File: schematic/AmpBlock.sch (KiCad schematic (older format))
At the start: 9 parts, among them U1 OPA454AIDDAR

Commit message: Added connectors to the library and made an array of lots of amps
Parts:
- renumbered C1 to C29, C3 to C30, C2 to C31, C4 to C32, R4 to R29, R5 to R30, R6 to R31, R7 to R32, U1 to U8
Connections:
- net labels added: INPUT_COM, OUTPUT_COM
- wire segments 32 -> 38
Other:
- note added: "In the LL schematic, the ground reference of the supply bypass capacitors are both what I call input_com\n"
- note added: "Should the E/D com also go to the local ground?"
- moved on the sheet: C3, R2

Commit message: Started adding footprints to library and started working on the layout of the amplifier block
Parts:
- C29, C30, C31, C32: footprint (none) -> Capacitor_SMD:C_0603_1608Metric
- R29, R30, R31, R32: footprint (none) -> Resistor_SMD:R_0603_1608Metric
- U8: footprint (none) -> ARTIQAmp:TI_SO-PowerPAD-8_ThermalVias
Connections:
- wire segments 38 -> 42
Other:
- moved on the sheet: C1, R1, R2
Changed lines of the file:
@@
 EESchema Schematic File Version 4
-LIBS:ARTIQAmp-cache
 EELAYER 29 0
 EELAYER END
 $Descr A4 11693 8268
 encoding utf-8
-Sheet 2 33
+Sheet 1 1
 Title "Amplifier block"
 Date ""
@@
 L Device:R R29
 U 1 1 5C968DBB
-P 4350 3350
+P 4300 3350
 AR Path="/5C968447/5C968DBB" Ref="R29"  Part="1"
 AR Path="/5C98A5A9/5C968DBB" Ref="R?"  Part="1"
@@
 AR Path="/5CAE2E6A/5C968DBB" Ref="R121"  Part="1"
 AR Path="/5CAE2EB0/5C968DBB" Ref="R125"  Part="1"
-F 0 "R1" V 4143 3350 50  0000 C CNN
-F 1 "49R9" V 4234 3350 50  0000 C CNN
-F 2 "" V 4280 3350 50  0001 C CNN
-F 3 "~" H 4350 3350 50  0001 C CNN
-	1    4350 3350
+AR Path="/5C968DBB" Ref="R1"  Part="1"
+F 0 "R1" V 4093 3350 50  0000 C CNN
+F 1 "49R9" V 4184 3350 50  0000 C CNN
+F 2 "Resistor_SMD:R_0603_1608Metric" V 4230 3350 50  0001 C CNN
+F 3 "~" H 4300 3350 50  0001 C CNN
+	1    4300 3350
 	0    1    1    0
 $EndComp
@@
 L Device:R R30
 U 1 1 5C969C02
-P 5000 4700
+P 4900 4700
 AR Path="/5C968447/5C969C02" Ref="R30"  Part="1"
 AR Path="/5C98A5A9/5C969C02" Ref="R?"  Part="1"
@@
 AR Path="/5CAE2E6A/5C969C02" Ref="R122"  Part="1"
 AR Path="/5CAE2EB0/5C969C02" Ref="R126"  Part="1"
-F 0 "R2" V 4900 4700 50  0000 L CNN
-F 1 "1.65k" V 5100 4700 50  0000 L CNN
-F 2 "" V 4930 4700 50  0001 C CNN
-F 3 "~" H 5000 4700 50  0001 C CNN
-	1    5000 4700
+AR Path="/5C969C02" Ref="R2"  Part="1"
+F 0 "R2" V 4800 4700 50  0000 L CNN
+F 1 "1.65k" V 5000 4700 50  0000 L CNN
+F 2 "Resistor_SMD:R_0603_1608Metric" V 4830 4700 50  0001 C CNN
+F 3 "~" H 4900 4700 50  0001 C CNN
+	1    4900 4700
 	0    1    1    0
 $EndComp
@@
 AR Path="/5CAE2E6A/5C96A29C" Ref="R124"  Part="1"
 AR Path="/5CAE2EB0/5C96A29C" Ref="R128"  Part="1"
+AR Path="/5C96A29C" Ref="R4"  Part="1"
 F 0 "R4" H 6780 3954 50  0000 R CNN
 F 1 "4.99k" H 6780 4045 50  0000 R CNN
-F 2 "" V 6780 4000 50  0001 C CNN
+F 2 "Resistor_SMD:R_0603_1608Metric" V 6780 4000 50  0001 C CNN
 F 3 "~" H 6850 4000 50  0001 C CNN
 	1    6850 4000
@@
 L Device:C C29
 U 1 1 5C96A628
-P 4750 3600
+P 4650 3600
 AR Path="/5C968447/5C96A628" Ref="C29"  Part="1"
 AR Path="/5C98A5A9/5C96A628" Ref="C?"  Part="1"
@@
 AR Path="/5CAE2E6A/5C96A628" Ref="C121"  Part="1"
 AR Path="/5CAE2EB0/5C96A628" Ref="C125"  Part="1"
-F 0 "C1" H 4865 3646 50  0000 L CNN
-F 1 "0.27uF" H 4865 3555 50  0000 L CNN
-F 2 "" H 4788 3450 50  0001 C CNN
-F 3 "~" H 4750 3600 50  0001 C CNN
-	1    4750 3600
+AR Path="/5C96A628" Ref="C1"  Part="1"
+F 0 "C1" H 4765 3646 50  0000 L CNN
+F 1 "0.27uF" H 4765 3555 50  0000 L CNN
+F 2 "Capacitor_SMD:C_0603_1608Metric" H 4688 3450 50  0001 C CNN
+F 3 "~" H 4650 3600 50  0001 C CNN
+	1    4650 3600
 	1    0    0    -1
 $EndComp
@@
 AR Path="/5CAE2E6A/5C96AF27" Ref="C124"  Part="1"
 AR Path="/5CAE2EB0/5C96AF27" Ref="C128"  Part="1"
+AR Path="/5C96AF27" Ref="C4"  Part="1"
 F 0 "C4" H 7365 4046 50  0000 L CNN
 F 1 "1.3nF" H 7365 3955 50  0000 L CNN
-F 2 "" H 7288 3850 50  0001 C CNN
+F 2 "Capacitor_SMD:C_0603_1608Metric" H 7288 3850 50  0001 C CNN
 F 3 "~" H 7250 4000 50  0001 C CNN
 	1    7250 4000
@@
 AR Path="/5CAE2E6A/5C96D358" Ref="U31"  Part="1"
 AR Path="/5CAE2EB0/5C96D358" Ref="U32"  Part="1"
+AR Path="/5C96D358" Ref="U1"  Part="1"
 F 0 "U1" H 6200 3450 50  0000 L CNN
 F 1 "OPA454AIDDAR" H 6150 3800 50  0000 L CNN
-F 2 "" H 5900 3600 50  0001 C CNN
+F 2 "ARTIQAmp:TI_SO-PowerPAD-8_ThermalVias" H 5900 3600 50  0001 C CNN
 F 3 "" H 5900 3600 50  0001 C CNN
 	1    5900 3600
@@
 AR Path="/5CAE2E6A/5C96EFD0" Ref="#PWR099"  Part="1"
 AR Path="/5CAE2EB0/5C96EFD0" Ref="#PWR0102"  Part="1"
-F 0 "#PWR09" H 5900 2350 50  0001 C CNN
+AR Path="/5C96EFD0" Ref="#PWR0102"  Part="1"
+F 0 "#PWR0102" H 5900 2350 50  0001 C CNN
 F 1 "VDD" H 5917 2673 50  0000 C CNN
 F 2 "" H 5900 2500 50  0001 C CNN
@@
 L power:VSS #PWR031
 U 1 1 5C96F7F1
-P 5900 4300
+P 5900 4450
 AR Path="/5C968447/5C96F7F1" Ref="#PWR031"  Part="1"
 AR Path="/5C98A5A9/5C96F7F1" Ref="#PWR?"  Part="1"
@@
 AR Path="/5CAE2E6A/5C96F7F1" Ref="#PWR0100"  Part="1"
 AR Path="/5CAE2EB0/5C96F7F1" Ref="#PWR0103"  Part="1"
-F 0 "#PWR010" H 5900 4150 50  0001 C CNN
-F 1 "VSS" H 5918 4473 50  0000 C CNN
-F 2 "" H 5900 4300 50  0001 C CNN
-F 3 "" H 5900 4300 50  0001 C CNN
-	1    5900 4300
+AR Path="/5C96F7F1" Ref="#PWR0103"  Part="1"
+F 0 "#PWR0103" H 5900 4300 50  0001 C CNN
+F 1 "VSS" H 5918 4623 50  0000 C CNN
+F 2 "" H 5900 4450 50  0001 C CNN
+F 3 "" H 5900 4450 50  0001 C CNN
+	1    5900 4450
 	-1   0    0    1
 $EndComp
@@
 AR Path="/5CAE2E6A/5C96FD85" Ref="C123"  Part="1"
 AR Path="/5CAE2EB0/5C96FD85" Ref="C127"  Part="1"
+AR Path="/5C96FD85" Ref="C3"  Part="1"
 F 0 "C3" V 5998 2700 50  0000 C CNN
 F 1 "0.1uF" V 6089 2700 50  0000 C CNN
-F 2 "" H 6288 2550 50  0001 C CNN
+F 2 "Capacitor_SMD:C_0603_1608Metric" H 6288 2550 50  0001 C CNN
 F 3 "~" H 6250 2700 50  0001 C CNN
 	1    6250 2700
@@
 AR Path="/5CAE2E6A/5C97026D" Ref="C122"  Part="1"
 AR Path="/5CAE2EB0/5C97026D" Ref="C126"  Part="1"
+AR Path="/5C97026D" Ref="C2"  Part="1"
 F 0 "C2" V 5898 4200 50  0000 C CNN
 F 1 "0.1uF" V 5989 4200 50  0000 C CNN
-F 2 "" H 6188 4050 50  0001 C CNN
+F 2 "Capacitor_SMD:C_0603_1608Metric" H 6188 4050 50  0001 C CNN
 F 3 "~" H 6150 4200 50  0001 C CNN
 	1    6150 4200
@@
 AR Path="/5CAE2E6A/5C9706CF" Ref="R123"  Part="1"
 AR Path="/5CAE2EB0/5C9706CF" Ref="R127"  Part="1"
+AR Path="/5C9706CF" Ref="R3"  Part="1"
 F 0 "R3" H 5900 2900 50  0000 R CNN
 F 1 "1M" H 5900 3000 50  0000 R CNN
-F 2 "" V 5630 2950 50  0001 C CNN
+F 2 "Resistor_SMD:R_0603_1608Metric" V 5630 2950 50  0001 C CNN
 F 3 "~" H 5700 2950 50  0001 C CNN
 	1    5700 2950
@@
 NoConn ~ 6100 3350
 Wire Wire Line
-	5300 3350 4750 3350
-Wire Wire Line
-	4750 3350 4750 3450
-Wire Wire Line
-	4750 3350 4500 3350
-Connection ~ 4750 3350
+	5300 3350 4650 3350
+Wire Wire Line
+	4650 3350 4650 3450
+Wire Wire Line
+	4650 3350 4450 3350
+Connection ~ 4650 3350
 $Comp
 L power:GND #PWR029
@@
 AR Path="/5CAE2E6A/5C971DB5" Ref="#PWR098"  Part="1"
 AR Path="/5CAE2EB0/5C971DB5" Ref="#PWR0101"  Part="1"
-F 0 "#PWR08" H 5700 3900 50  0001 C CNN
+AR Path="/5C971DB5" Ref="#PWR0101"  Part="1"
+F 0 "#PWR0101" H 5700 3900 50  0001 C CNN
 F 1 "GND" H 5705 3977 50  0000 C CNN
 F 2 "" H 5700 4150 50  0001 C CNN
@@
 Connection ~ 5900 4200
 Wire Wire Line
-	5900 4200 5900 4300
+	5900 4200 5900 4400
 Wire Wire Line
 	5900 2500 5900 2700
@@
 	6850 4150 6850 4700
 Wire Wire Line
-	6850 4700 5200 4700
-Wire Wire Line
-	5200 4700 5200 3850
-Wire Wire Line
-	5200 3850 5300 3850
+	6850 4700 5150 4700
+Wire Wire Line
+	5150 4700 5150 3850
+Wire Wire Line
+	5150 3850 5300 3850
 Wire Wire Line
 	7250 4150 7250 4700
@@
 Connection ~ 6850 4700
 Wire Wire Line
-	5200 4700 5150 4700
-Wire Wire Line
-	4100 4700 4750 4700
-Wire Wire Line
-	4750 3750 4750 4700
-Text HLabel 4100 3350 0    50   Input ~ 0
+	5150 4700 5050 4700
+Wire Wire Line
+	4050 4700 4650 4700
+Wire Wire Line
+	4650 3750 4650 4700
+Text HLabel 4050 3350 0    50   Input ~ 0
 INPUT
 Text HLabel 8000 3600 2    50   Input ~ 0
 OUTPUT
 Wire Wire Line
-	4200 3350 4100 3350
+	4150 3350 4050 3350
 Wire Wire Line
 	7250 3600 8000 3600
@@
 Text Notes 2500 5800 0    50   ~ 0
 ToDo:\n>Tweak the value of the input resistor\n>Tweak the value of the ouptut capacitor\n>Add a connection for the power pad of the chip
-Text HLabel 4100 4700 0    50   Input ~ 0
+Text HLabel 4050 4700 0    50   Input ~ 0
 INPUT_COM
 Text Notes 6350 2350 0    50   ~ 0
@@
 Text HLabel 8000 4700 2    50   Input ~ 0
 OUTPUT_COM
-Connection ~ 5200 4700
-Connection ~ 4750 4700
-Wire Wire Line
-	4750 4700 4850 4700
+Connection ~ 5150 4700
+Connection ~ 4650 4700
+Wire Wire Line
+	4650 4700 4750 4700
 Wire Wire Line
 	8000 4700 7650 4700
@@
 	7650 4950 6600 4950
 Wire Wire Line
-	4750 4950 4750 4700
+	4650 4950 4650 4700
 Wire Wire Line
 	5900 2700 5900 3250
@@
 Connection ~ 6600 4950
 Wire Wire Line
-	6600 4950 4750 4950
+	6600 4950 4650 4950
 Wire Wire Line
 	6100 2700 5900 2700
 Text Notes 5700 5300 0    50   ~ 0
 Should the E/D com also go to the local ground?
+Wire Wire Line
+	5300 3600 5250 3600
+Wire Wire Line
+	5250 3600 5250 4400
+Wire Wire Line
+	5250 4400 5900 4400
+Connection ~ 5900 4400
+Wire Wire Line
+	5900 4400 5900 4450
 $EndSCHEMATC

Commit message: Test a dumb little edit from the linux machine on campus
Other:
- note added: "This is just a dumb little note for me to check pushing from Linux and pulling from Windows"
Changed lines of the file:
@@
 EESchema Schematic File Version 4
-EELAYER 29 0
+EELAYER 30 0
 EELAYER END
 $Descr A4 11693 8268
 encoding utf-8
-Sheet 1 1
+Sheet 18 33
 Title "Amplifier block"
 Date ""
@@
 AR Path="/5CAE2EB0/5C968DBB" Ref="R125"  Part="1"
 AR Path="/5C968DBB" Ref="R1"  Part="1"
-F 0 "R1" V 4093 3350 50  0000 C CNN
+F 0 "R65" V 4093 3350 50  0000 C CNN
 F 1 "49R9" V 4184 3350 50  0000 C CNN
 F 2 "Resistor_SMD:R_0603_1608Metric" V 4230 3350 50  0001 C CNN
@@
 AR Path="/5CAE2EB0/5C969C02" Ref="R126"  Part="1"
 AR Path="/5C969C02" Ref="R2"  Part="1"
-F 0 "R2" V 4800 4700 50  0000 L CNN
+F 0 "R66" V 4800 4700 50  0000 L CNN
 F 1 "1.65k" V 5000 4700 50  0000 L CNN
 F 2 "Resistor_SMD:R_0603_1608Metric" V 4830 4700 50  0001 C CNN
@@
 AR Path="/5CAE2EB0/5C96A29C" Ref="R128"  Part="1"
 AR Path="/5C96A29C" Ref="R4"  Part="1"
-F 0 "R4" H 6780 3954 50  0000 R CNN
+F 0 "R68" H 6780 3954 50  0000 R CNN
 F 1 "4.99k" H 6780 4045 50  0000 R CNN
 F 2 "Resistor_SMD:R_0603_1608Metric" V 6780 4000 50  0001 C CNN
@@
 AR Path="/5CAE2EB0/5C96A628" Ref="C125"  Part="1"
 AR Path="/5C96A628" Ref="C1"  Part="1"
-F 0 "C1" H 4765 3646 50  0000 L CNN
+F 0 "C65" H 4765 3646 50  0000 L CNN
 F 1 "0.27uF" H 4765 3555 50  0000 L CNN
 F 2 "Capacitor_SMD:C_0603_1608Metric" H 4688 3450 50  0001 C CNN
@@
 AR Path="/5CAE2EB0/5C96AF27" Ref="C128"  Part="1"
 AR Path="/5C96AF27" Ref="C4"  Part="1"
-F 0 "C4" H 7365 4046 50  0000 L CNN
+F 0 "C68" H 7365 4046 50  0000 L CNN
 F 1 "1.3nF" H 7365 3955 50  0000 L CNN
 F 2 "Capacitor_SMD:C_0603_1608Metric" H 7288 3850 50  0001 C CNN
@@
 AR Path="/5CAE2EB0/5C96D358" Ref="U32"  Part="1"
 AR Path="/5C96D358" Ref="U1"  Part="1"
-F 0 "U1" H 6200 3450 50  0000 L CNN
+F 0 "U17" H 6200 3450 50  0000 L CNN
 F 1 "OPA454AIDDAR" H 6150 3800 50  0000 L CNN
 F 2 "ARTIQAmp:TI_SO-PowerPAD-8_ThermalVias" H 5900 3600 50  0001 C CNN
@@
 AR Path="/5CAE2EB0/5C96EFD0" Ref="#PWR0102"  Part="1"
 AR Path="/5C96EFD0" Ref="#PWR0102"  Part="1"
-F 0 "#PWR0102" H 5900 2350 50  0001 C CNN
+F 0 "#PWR057" H 5900 2350 50  0001 C CNN
 F 1 "VDD" H 5917 2673 50  0000 C CNN
 F 2 "" H 5900 2500 50  0001 C CNN
@@
 AR Path="/5CAE2EB0/5C96F7F1" Ref="#PWR0103"  Part="1"
 AR Path="/5C96F7F1" Ref="#PWR0103"  Part="1"
-F 0 "#PWR0103" H 5900 4300 50  0001 C CNN
+F 0 "#PWR058" H 5900 4300 50  0001 C CNN
 F 1 "VSS" H 5918 4623 50  0000 C CNN
 F 2 "" H 5900 4450 50  0001 C CNN
@@
 AR Path="/5CAE2EB0/5C96FD85" Ref="C127"  Part="1"
 AR Path="/5C96FD85" Ref="C3"  Part="1"
-F 0 "C3" V 5998 2700 50  0000 C CNN
+F 0 "C67" V 5998 2700 50  0000 C CNN
 F 1 "0.1uF" V 6089 2700 50  0000 C CNN
 F 2 "Capacitor_SMD:C_0603_1608Metric" H 6288 2550 50  0001 C CNN
@@
 AR Path="/5CAE2EB0/5C97026D" Ref="C126"  Part="1"
 AR Path="/5C97026D" Ref="C2"  Part="1"
-F 0 "C2" V 5898 4200 50  0000 C CNN
+F 0 "C66" V 5898 4200 50  0000 C CNN
 F 1 "0.1uF" V 5989 4200 50  0000 C CNN
 F 2 "Capacitor_SMD:C_0603_1608Metric" H 6188 4050 50  0001 C CNN
@@
 AR Path="/5CAE2EB0/5C9706CF" Ref="R127"  Part="1"
 AR Path="/5C9706CF" Ref="R3"  Part="1"
-F 0 "R3" H 5900 2900 50  0000 R CNN
+F 0 "R67" H 5900 2900 50  0000 R CNN
 F 1 "1M" H 5900 3000 50  0000 R CNN
 F 2 "Resistor_SMD:R_0603_1608Metric" V 5630 2950 50  0001 C CNN
@@
 AR Path="/5CAE2EB0/5C971DB5" Ref="#PWR0101"  Part="1"
 AR Path="/5C971DB5" Ref="#PWR0101"  Part="1"
-F 0 "#PWR0101" H 5700 3900 50  0001 C CNN
+F 0 "#PWR056" H 5700 3900 50  0001 C CNN
 F 1 "GND" H 5705 3977 50  0000 C CNN
 F 2 "" H 5700 4150 50  0001 C CNN
@@
 Wire Wire Line
 	5900 4400 5900 4450
+Text Notes 1450 2150 0    50   ~ 0
+This is just a dumb little note for me to check pushing from Linux and pulling from Windows
 $EndSCHEMATC

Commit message: Add power connections; assign footprints to all components
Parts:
- renumbered C31 to C35, C29 to C36, C32 to C37, C30 to C38, R31 to R29, R29 to R30, R32 to R31, R30 to R32
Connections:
- net labels added: +48V, -48V
- net labels removed: VDD, VSS
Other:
- note removed: "This is just a dumb little note for me to check pushing from Linux and pulling from Windows"

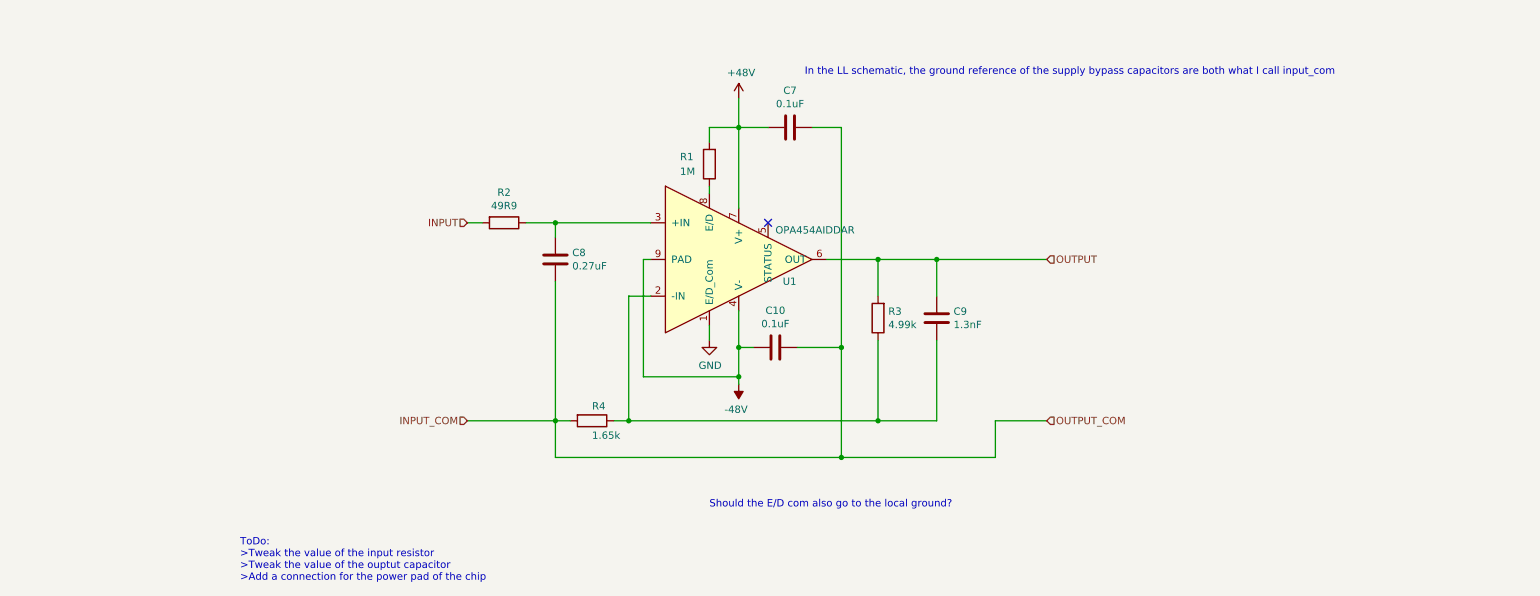
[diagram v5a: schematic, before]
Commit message: Update libraries for new components
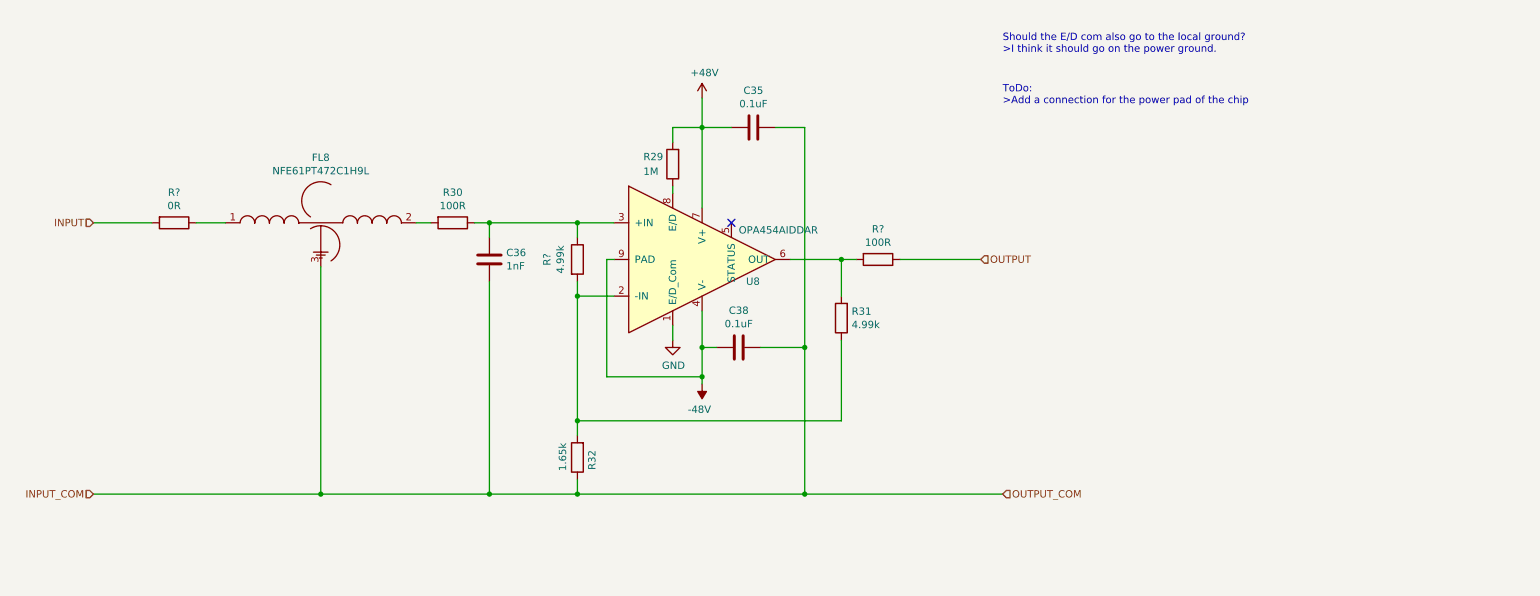
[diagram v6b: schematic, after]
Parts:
- removed C37: 1.3nF, Capacitor_SMD:C_0603_1608Metric, symbol Device:C
- added FL26: NFE61PT472C1H9L, ARTIQAmp:NFE61, symbol ARTIQAmp:NFE61PT472C1H9L
- added R?: 0R, Resistor_SMD:R_0603_1608Metric, symbol Device:R
- added R?: 4.99k, Resistor_SMD:R_0603_1608Metric, symbol Device:R
- added R?: 100R, Resistor_SMD:R_0603_1608Metric, symbol Device:R
- C36: value 0.27uF -> 1nF
- R30: value 49R9 -> 100R
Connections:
- net INPUT: now also R?.2; no longer R30.2
- net INPUT_COM: now also R32.1, FL26.3; no longer R32.2
- net OUTPUT: now also R?.1; no longer R31.2, U8.6 (OUT)
- net at C36.1, R30.1, U8.3 (+IN): now also R?.1
- net at R31.1, U8.2 (-IN): now also R32.2, R?.2; no longer R32.1
- new net: FL26.2, R30.2
- new net: R31.2, R?.2, U8.6 (OUT)
- new net: FL26.1, R?.1
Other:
- note added: "Should the E/D com also go to the local ground?\n>I think it should go on the power ground.\n"
- note added: "ToDo:\n>Add a connection for the power pad of the chip"
- note removed: "In the LL schematic, the ground reference of the supply bypass capacitors are both what I call input_com\n"
- note removed: "Should the E/D com also go to the local ground?"
- note removed: "ToDo:\n>Tweak the value of the input resistor\n>Tweak the value of the ouptut capacitor\n>Add a connection for the power pad of the chip"
- moved on the sheet: C35, C36, C38, R29, R30, R31, R32, U8

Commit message: Initial updates to schematic with new components
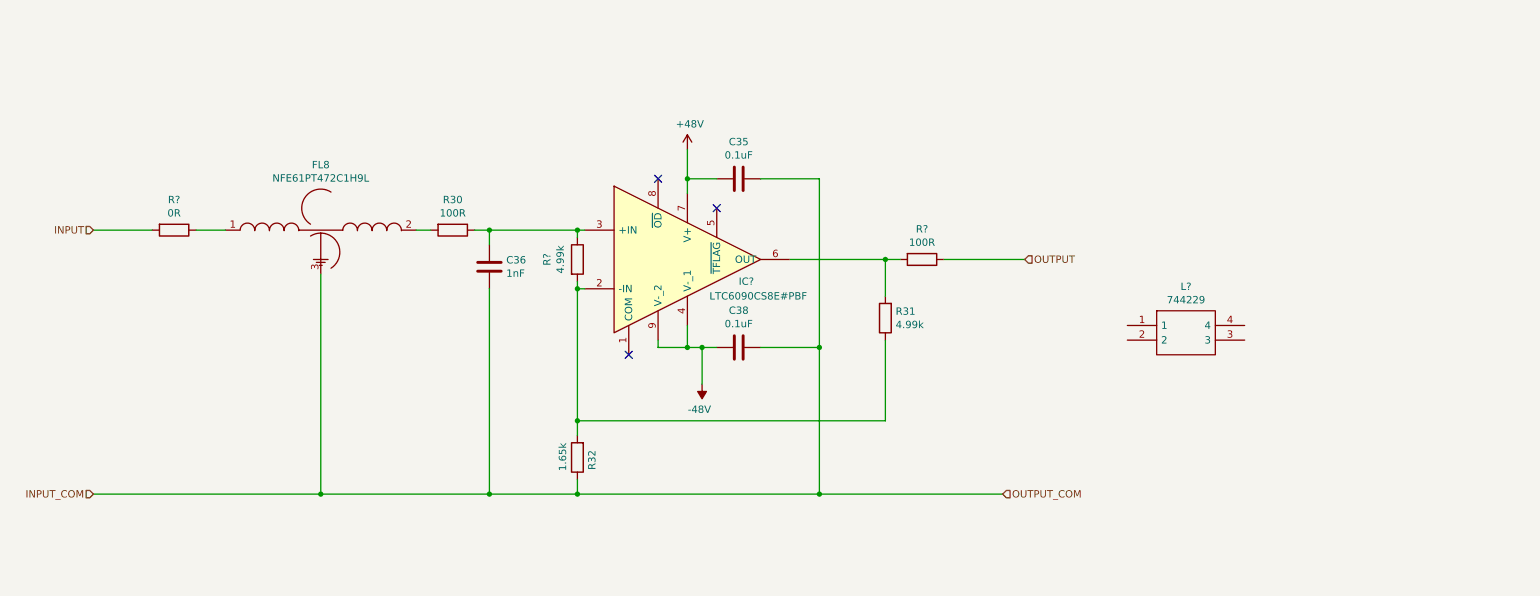
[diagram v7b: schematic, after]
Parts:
- removed R29: 1M, Resistor_SMD:R_0603_1608Metric, symbol Device:R
- removed U8: OPA454AIDDAR, ARTIQAmp:TI_SO-PowerPAD-8_ThermalVias, symbol ARTIQAmp:OPA454AIDDAR
- added IC?: LTC6090CS8E#PBF, SOIC127P599X175-9N, symbol ARTIQAmp:LTC6090CS8E#PBF
- added L?: 744229, WE-SL575, symbol ARTIQAmp:744229
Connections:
- net +48V: now also IC?.7 (V+)
- net -48V: now also IC?.4 (V-_1), IC?.9 (V-_2)
- net at C36.1, R30.1, R?.1: now also IC?.3 (+IN)
- net at R31.1, R32.2, R?.2: now also IC?.2 (-IN)
- net at R31.2, R?.2: now also IC?.6 (OUT)
- no-connect marks 1 -> 3
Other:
- note removed: "Should the E/D com also go to the local ground?\n>I think it should go on the power ground.\n"
- note removed: "ToDo:\n>Add a connection for the power pad of the chip"
- moved on the sheet: C35, C36, FL8, R30, R31, R?
